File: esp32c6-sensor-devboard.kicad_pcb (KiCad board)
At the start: 4 copper layers, 90 x 50 mm, 193 parts, among them J1 Conn_01x04_Pin, J2 Micro_SD_Card_Det1, J3 Screw_Terminal_01x02, J4 USB_C_Receptacle_USB2.0_14P, J5 Screw_Terminal_01x02, J6 Screw_Terminal_01x06, J7 Screw_Terminal_01x04, J8 Conn_01x04_Pin, J9 Conn_01x03_Pin, SW1 SW_Push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

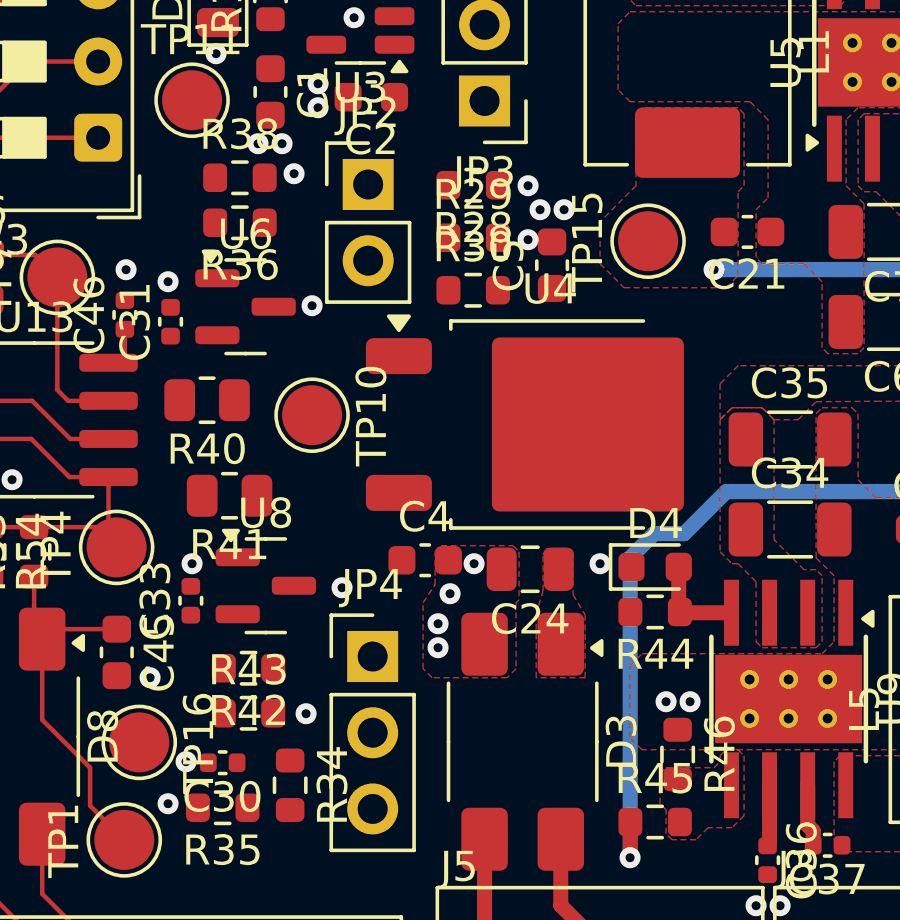
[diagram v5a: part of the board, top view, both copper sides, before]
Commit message: pcb: add 10/20v ldo routing
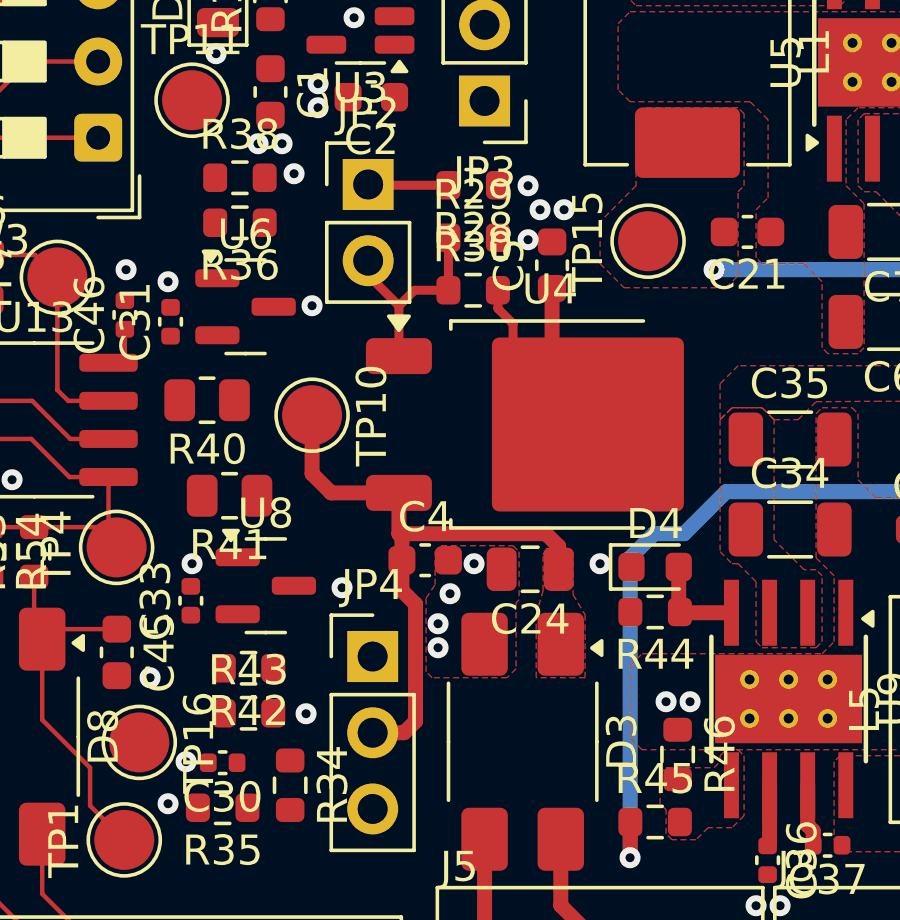
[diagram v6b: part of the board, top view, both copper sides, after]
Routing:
- net +12/24DC: track 0.00 -> 20.7 mm
- net +10/20DC: track 4.74 -> 15.5 mm
- net Net-(JP2-B): track 0.00 -> 7.22 mm
- net Net-(JP2-A): track 0.00 -> 2.69 mm

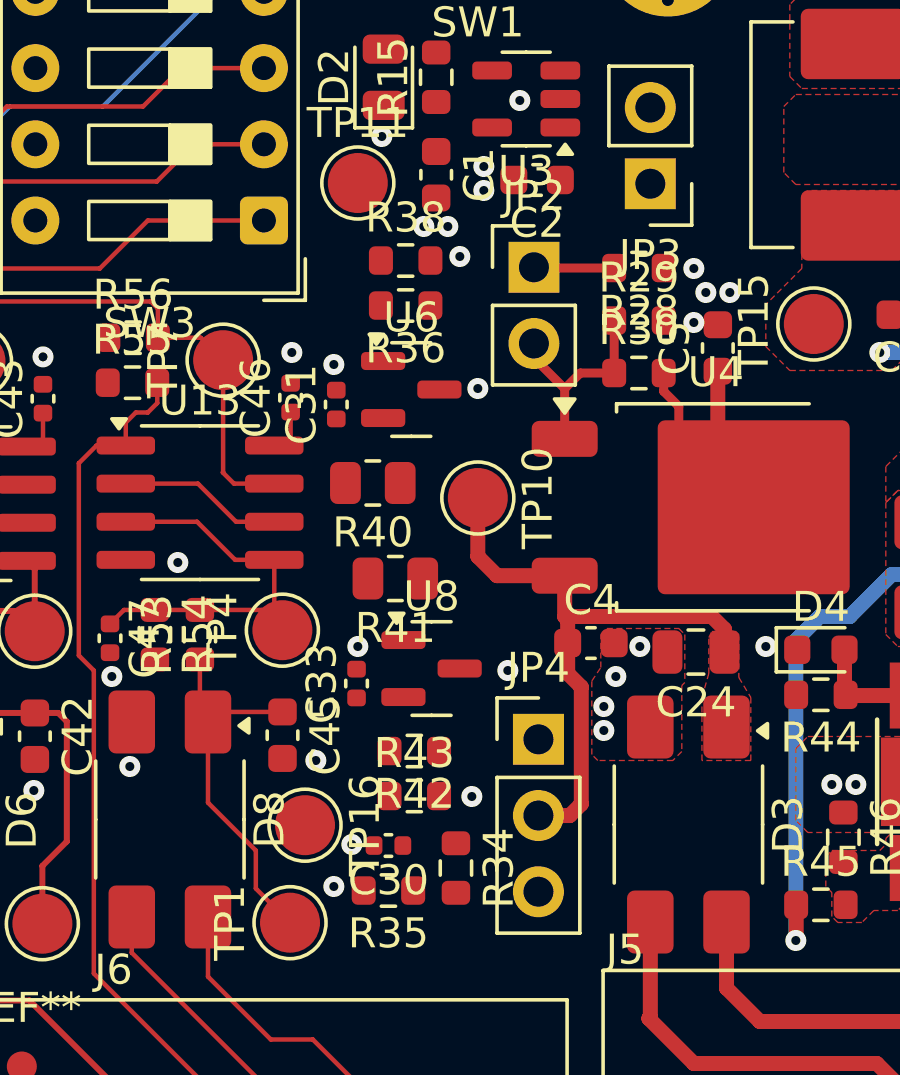
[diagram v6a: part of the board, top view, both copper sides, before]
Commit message: pcb: 24/12v shunt regulators routing
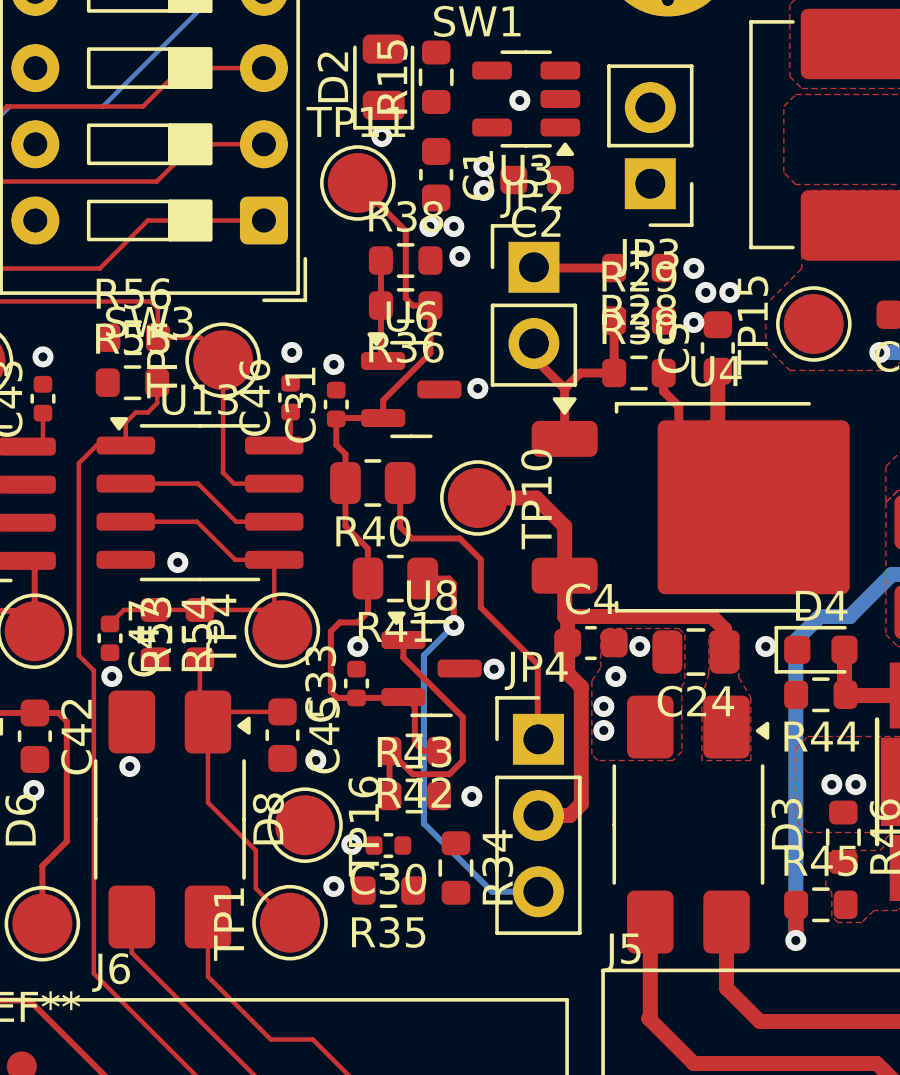
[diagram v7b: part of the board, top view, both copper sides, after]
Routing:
- net /Vlogic: track 0.00 -> 27.0 mm
- net Net-(JP4-B): track 0.00 -> 14.3 mm, vias 0 -> 1
- net Net-(JP4-A): track 0.00 -> 11.4 mm
- net Net-(U8-REF): track 0.00 -> 9.29 mm
- net Net-(U6-REF): track 0.00 -> 3.38 mm

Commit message: pcb: comparator routing
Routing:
- net Net-(J8-Pin_1): track 0.00 -> 14.3 mm, vias 0 -> 1
- net /Power/+24VDC: track 23.3 -> 31.1 mm
- net /Vref: track 16.4 -> 23.3 mm
- net +12/24DC: track 20.6 -> 23.7 mm
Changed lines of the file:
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@@
 	)
 	(segment
+		(start 194.27 99.759385)
+		(end 196.095 99.759385)
+		(width 0.3)
+		(layer "F.Cu")
+		(net 5)
+	)
+	(segment
 		(start 197.895 90.839385)
 		(end 197.895 89.195)
@@
 	)
 	(segment
+		(start 196.095 99.759385)
+		(end 197.02 98.834385)
+		(width 0.3)
+		(layer "F.Cu")
+		(net 5)
+	)
+	(segment
 		(start 203.22 92.62)
 		(end 202.8 92.2)
@@
 	)
 	(segment
+		(start 192.845 100.645)
+		(end 192.845 101.334385)
+		(width 0.3)
+		(layer "F.Cu")
+		(net 18)
+	)
+	(segment
 		(start 171.71 89.100615)
 		(end 169.900615 89.100615)
@@
 	)
 	(segment
+		(start 192.5 99.834385)
+		(end 192.5 99.4)
+		(width 0.3)
+		(layer "F.Cu")
+		(net 18)
+	)
+	(segment
+		(start 192.5 99.834385)
+		(end 192.5 100.3)
+		(width 0.3)
+		(layer "F.Cu")
+		(net 18)
+	)
+	(segment
+		(start 194.27 101.409385)
+		(end 192.92 101.409385)
+		(width 0.3)
+		(layer "F.Cu")
+		(net 18)
+	)
+	(segment
+		(start 192.5 100.3)
+		(end 192.845 100.645)
+		(width 0.3)
+		(layer "F.Cu")
+		(net 18)
+	)
+	(segment
+		(start 189.24723 99.149)
+		(end 189.24 99.15623)
+		(width 0.3)
+		(layer "F.Cu")
+		(net 18)
+	)
+	(segment
 		(start 178.175615 89.075615)
 		(end 176.905615 87.805615)
@@
 	)
 	(segment
+		(start 192.92 101.409385)
+		(end 192.845 101.334385)
+		(width 0.3)
+		(layer "F.Cu")
+		(net 18)
+	)
+	(segment
 		(start 176.905615 87.805615)
 		(end 175.01 87.805615)
@@
 	)
 	(segment
+		(start 192.249 99.149)
+		(end 189.24723 99.149)
+		(width 0.3)
+		(layer "F.Cu")
+		(net 18)
+	)
+	(segment
 		(start 169.900615 89.100615)
 		(end 168.630615 87.830615)
@@
 	)
 	(segment
+		(start 192.5 99.4)
+		(end 192.249 99.149)
+		(width 0.3)
+		(layer "F.Cu")
+		(net 18)
+	)
+	(segment
 		(start 190.9575 94.914385)
 		(end 192.49 94.914385)
@@
 	)
 	(segment
+		(start 206.825 104.225)
+		(end 206.825 110.2975)
+		(width 0.5)
+		(layer "B.Cu")
+		(net 24)
+	)
+	(segment
 		(start 206.4 92.2)
 		(end 207.4 92.2)
@@
 	)
 	(segment
+		(start 205.6 103)
+		(end 206.825 104.225)
+		(width 0.5)
+		(layer "B.Cu")
+		(net 24)
+	)
+	(segment
 		(start 208.8 90.8)
 		(end 216.8 90.8)
@@
 	)
 	(segment
+		(start 146.8625 96.8375)
+		(end 146.8625 96.3)
+		(width 0.15)
+		(layer "F.Cu")
+		(net 62)
+	)
+	(segment
+		(start 146.2 97.5)
+		(end 146.8625 96.8375)
+		(width 0.15)
+		(layer "F.Cu")
+		(net 62)
+	)
+	(via
+		(at 146.2 97.5)
+		(size 0.5)
+		(drill 0.3)
+		(layers "F.Cu" "B.Cu")
+		(net 62)
+	)
+	(segment
+		(start 134.25 97.42)
+		(end 135.32 97.42)
+		(width 0.15)
+		(layer "B.Cu")
+		(net 62)
+	)
+	(segment
+		(start 145.2 98.5)
+		(end 146.2 97.5)
+		(width 0.15)
+		(layer "B.Cu")
+		(net 62)
+	)
+	(segment
+		(start 136.4 98.5)
+		(end 145.2 98.5)
+		(width 0.15)
+		(layer "B.Cu")
+		(net 62)
+	)
+	(segment
+		(start 135.32 97.42)
+		(end 136.4 98.5)
+		(width 0.15)
+		(layer "B.Cu")
+		(net 62)
+	)
+	(segment
